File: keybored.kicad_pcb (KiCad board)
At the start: 2 copper layers, 316.7 x 133.3 mm, 202 parts, among them J1 USB_C_Receptacle_USB2.0, J2 ISP, J3 Conn_01x03, J4 Conn_01x03, K1 KEYSW, K10 KEYSW, K11 KEYSW, K12 KEYSW, K13 KEYSW, K14 KEYSW, K15 KEYSW, K16 KEYSW, K17 KEYSW, K18 KEYSW, K19 KEYSW, K2 KEYSW, K20 KEYSW, K21 KEYSW, K22 KEYSW, K23 KEYSW, K24 KEYSW, K25 KEYSW, K26 KEYSW, K27 KEYSW, K28 KEYSW, K29 KEYSW, K3 KEYSW, K30 KEYSW, K31 KEYSW, K32 KEYSW, K33 KEYSW, K34 KEYSW, K35 KEYSW, K36 KEYSW, K37 KEYSW, K38 KEYSW, K39 KEYSW, K4 KEYSW, K40 KEYSW, K41 KEYSW, K42 KEYSW, K43 KEYSW, K44 KEYSW, K45 KEYSW, K46 KEYSW, K47 KEYSW, K48 KEYSW, K49 KEYSW, K5 KEYSW, K50 KEYSW, K51 KEYSW, K52 KEYSW, K53 KEYSW, K54 KEYSW, K55 KEYSW, K56 KEYSW, K57 KEYSW, K58 KEYSW, K59 KEYSW, K6 KEYSW, K60 KEYSW, K61 KEYSW, K62 KEYSW, K63 KEYSW, K64 KEYSW, K65 KEYSW, K66 KEYSW, K7 KEYSW, K8 KEYSW, K9 KEYSW, SW1 SW_PUSH, SW2 Rot_Enc_Sw, U1 ATMEGA32U4, U2 SSD1306-Display_Graphic, Y1 Crystal

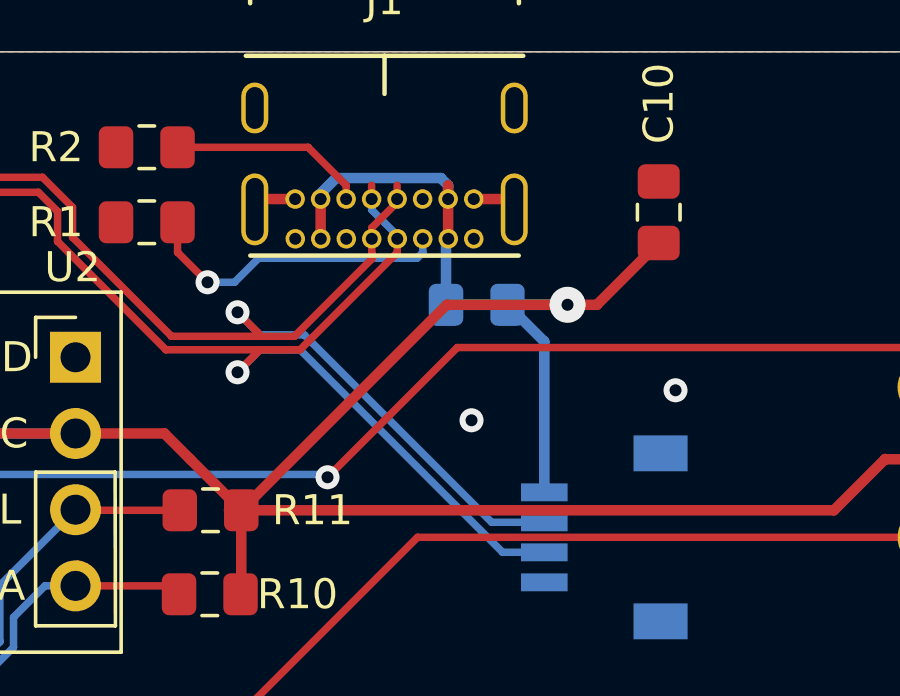
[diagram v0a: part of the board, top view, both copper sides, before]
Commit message: Updates to keyboard PCB and Plate
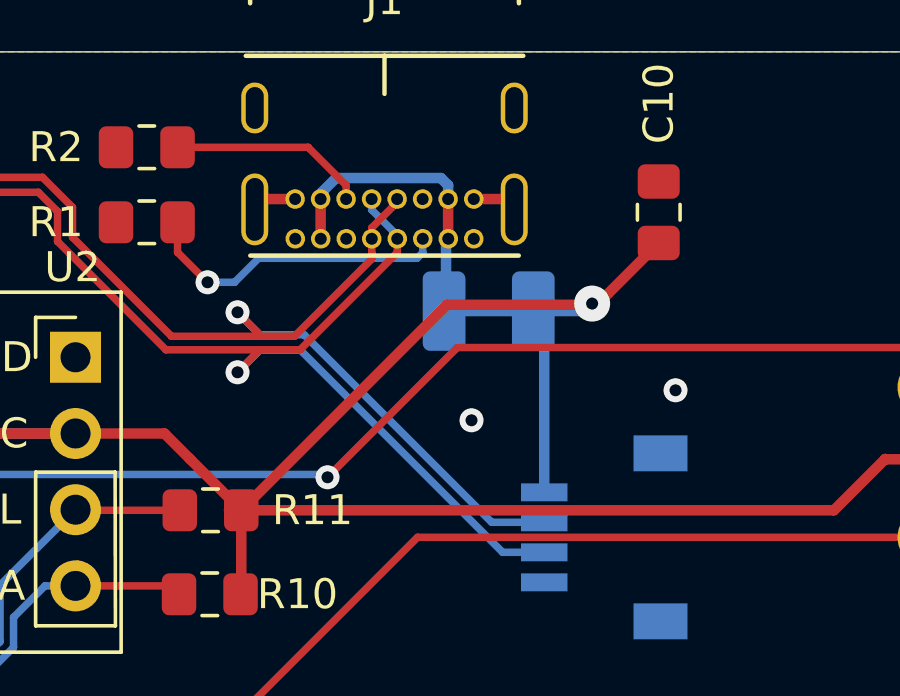
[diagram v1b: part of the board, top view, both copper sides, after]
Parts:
- removed the REF** at (340.0, 82.2)
- added REF**: Polyfuse, Fuse:Fuse_1210_3225Metric_Pad1.42x2.65mm_HandSolder, B.Cu at (340.4, 82.5)
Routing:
- net VCC: track 1050.1 -> 1048.9 mm
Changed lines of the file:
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@@
     (thickness 1.6)
     (drawings 108)
-    (tracks 2958)
+    (tracks 2956)
     (zones 0)
     (modules 202)
@@
     (mod_text_size 1 1)
     (mod_text_width 0.15)
-    (pad_size 1.15 1.4)
+    (pad_size 1.425 2.65)
     (pad_drill 0)
     (pad_to_mask_clearance 0.05)
@@
     (add_net VCC)
   )
+  (module Fuse:Fuse_1210_3225Metric_Pad1.42x2.65mm_HandSolder (layer B.Cu)
+    (at 340.3725 82.46)
+    (descr "Fuse SMD 1210 (3225 Metric), square (rectangular) end terminal, IPC_7351 nominal with elongated pad for handsoldering. (Body size source: http://www.tortai-tech.com/upload/download/2011102023233369053.pdf), generated with kicad-footprint-generator")
+    (tags "resistor handsolder")
+    (attr smd)
+    (fp_text reference REF** (at 0 2.28) (layer B.SilkS) hide
+      (effects (font (size 1 1) (thickness 0.15)) (justify mirror))
+    )
+    (fp_text value Polyfuse (at 0 -2.28) (layer B.Fab)
+      (effects (font (size 1 1) (thickness 0.15)) (justify mirror))
+    )
+    (fp_line (start 2.45 -1.58) (end -2.45 -1.58) (layer B.CrtYd) (width 0.05))
+    (fp_line (start 2.45 1.58) (end 2.45 -1.58) (layer B.CrtYd) (width 0.05))
+    (fp_line (start -2.45 1.58) (end 2.45 1.58) (layer B.CrtYd) (width 0.05))
+    (fp_line (start -2.45 -1.58) (end -2.45 1.58) (layer B.CrtYd) (width 0.05))
+    (fp_line (start -0.602064 -1.36) (end 0.602064 -1.36) (layer B.SilkS) (width 0.12))
+    (fp_line (start -0.602064 1.36) (end 0.602064 1.36) (layer B.SilkS) (width 0.12))
+    (fp_line (start 1.6 -1.25) (end -1.6 -1.25) (layer B.Fab) (width 0.1))
+    (fp_line (start 1.6 1.25) (end 1.6 -1.25) (layer B.Fab) (width 0.1))
+    (fp_line (start -1.6 1.25) (end 1.6 1.25) (layer B.Fab) (width 0.1))
+    (fp_line (start -1.6 -1.25) (end -1.6 1.25) (layer B.Fab) (width 0.1))
+    (fp_text user %R (at 0 0) (layer B.Fab)
+      (effects (font (size 0.8 0.8) (thickness 0.12)) (justify mirror))
+    )
+    (pad 2 smd roundrect (at 1.4875 0) (size 1.425 2.65) (layers B.Cu B.Paste B.Mask) (roundrect_rratio 0.175)
+      (net 77 VCC))
+    (pad 1 smd roundrect (at -1.4875 0) (size 1.425 2.65) (layers B.Cu B.Paste B.Mask) (roundrect_rratio 0.175439)
+      (net 77 VCC))
+    (model ${KISYS3DMOD}/Fuse.3dshapes/Fuse_1210_3225Metric.wrl
+      (at (xyz 0 0 0))
+      (scale (xyz 1 1 1))
+      (rotate (xyz 0 0 0))
+    )
+  )
   (module keybored:floppy_disks_2 (layer B.Cu)
     (at 255 83.75 180)
@@
       (net 79 USB_D+))
   )
-  (module Fuse:Fuse_0805_2012Metric_Pad1.15x1.40mm_HandSolder locked (layer B.Cu)
-    (at 339.975 82.25)
-    (descr "Fuse SMD 0805 (2012 Metric), square (rectangular) end terminal, IPC_7351 nominal with elongated pad for handsoldering. (Body size source: https://docs.google.com/spreadsheets/d/1BsfQQcO9C6DZCsRaXUlFlo91Tg2WpOkGARC1WS5S8t0/edit?usp=sharing), generated with kicad-footprint-generator")
-    (tags "resistor handsolder")
-    (attr smd)
-    (fp_text reference REF** (at 4 0) (layer B.SilkS) hide
-      (effects (font (size 1 1) (thickness 0.15)) (justify mirror))
-    )
-    (fp_text value Fuse_0805 (at 0 -1.5) (layer B.Fab) hide
-      (effects (font (size 1 1) (thickness 0.15)) (justify mirror))
-    )
-    (fp_line (start -1 -0.6) (end -1 0.6) (layer B.Fab) (width 0.1))
-    (fp_line (start -1 0.6) (end 1 0.6) (layer B.Fab) (width 0.1))
-    (fp_line (start 1 0.6) (end 1 -0.6) (layer B.Fab) (width 0.1))
-    (fp_line (start 1 -0.6) (end -1 -0.6) (layer B.Fab) (width 0.1))
-    (fp_line (start -0.261252 0.71) (end 0.261252 0.71) (layer B.SilkS) (width 0.12))
-    (fp_line (start -0.261252 -0.71) (end 0.261252 -0.71) (layer B.SilkS) (width 0.12))
-    (fp_line (start -1.85 -0.95) (end -1.85 0.95) (layer B.CrtYd) (width 0.05))
-    (fp_line (start -1.85 0.95) (end 1.85 0.95) (layer B.CrtYd) (width 0.05))
-    (fp_line (start 1.85 0.95) (end 1.85 -0.95) (layer B.CrtYd) (width 0.05))
-    (fp_line (start 1.85 -0.95) (end -1.85 -0.95) (layer B.CrtYd) (width 0.05))
-    (fp_text user %R (at 0 0) (layer B.Fab)
-      (effects (font (size 0.5 0.5) (thickness 0.08)) (justify mirror))
-    )
-    (pad 2 smd roundrect (at 1.025 0) (size 1.15 1.4) (layers B.Cu B.Paste B.Mask) (roundrect_rratio 0.217)
-      (net 77 VCC))
-    (pad 1 smd roundrect (at -1.025 0) (size 1.15 1.4) (layers B.Cu B.Paste B.Mask) (roundrect_rratio 0.217)
-      (net 77 VCC))
-    (model ${KISYS3DMOD}/Fuse.3dshapes/Fuse_0805_2012Metric.wrl
-      (at (xyz 0 0 0))
-      (scale (xyz 1 1 1))
-      (rotate (xyz 0 0 0))
-    )
-  )
   (module keybored:sadge_decal (layer B.Cu)
     (at 160.5 193.5 180)
@@
   (gr_circle (center 216.69375 214.3125) (end 219.075 214.3125) (layer Dwgs.User) (width 0.15))
   (gr_circle (center 100.0125 214.3125) (end 102.39375 214.3125) (layer Dwgs.User) (width 0.15))
-  (gr_text GND (at 316.3 99.2 90) (layer B.SilkS)
+  (gr_text GND (at 311 99.2 90) (layer B.SilkS)
     (effects (font (size 1 1) (thickness 0.15)) (justify mirror))
   )
@@
     (effects (font (size 1 1) (thickness 0.15)) (justify mirror))
   )
-  (gr_text +5V (at 311.3 99.1 90) (layer B.SilkS)
+  (gr_text +5V (at 316.2 99.1 90) (layer B.SilkS)
     (effects (font (size 1 1) (thickness 0.15)) (justify mirror))
   )
@@
   (segment (start 106.75 104.05) (end 111.46999 108.76999) (width 0.25) (layer B.Cu) (net 76))
   (segment (start 106.75 99.29) (end 106.75 104.05) (width 0.25) (layer B.Cu) (net 76))
-  (via (at 343 82.25) (size 1.2) (drill 0.4) (layers F.Cu B.Cu) (net 77))
+  (via (at 343.82 82.21) (size 1.2) (drill 0.4) (layers F.Cu B.Cu) (net 77))
   (segment (start 282.99325 88.032233) (end 283.477359 87.548124) (width 0.25) (layer F.Cu) (net 77))
   (segment (start 269.922641 92.051876) (end 270.40675 91.567767) (width 0.25) (layer F.Cu) (net 77))
@@
   (segment (start 334.77 78.725) (end 334.77 80.045) (width 0.35) (layer F.Cu) (net 77))
   (segment (start 346.04 79.81826) (end 346.04 80.19) (width 0.35) (layer F.Cu) (net 77))
-  (segment (start 339.02 78.725) (end 339.02 78.265381) (width 0.35) (layer F.Cu) (net 77))
   (segment (start 293.234999 78.424999) (end 291.92 77.11) (width 0.35) (layer B.Cu) (net 77))
   (segment (start 293.234999 81.384999) (end 293.234999 78.424999) (width 0.35) (layer B.Cu) (net 77))
@@
   (segment (start 338.95 80.125) (end 339.025 80.05) (width 0.35) (layer B.Cu) (net 77))
   (segment (start 338.95 82.25) (end 338.997002 82.25) (width 0.35) (layer B.Cu) (net 77))
-  (segment (start 338.95 82.25) (end 341 82.25) (width 0.35) (layer B.Cu) (net 77))
-  (segment (start 342.225 83.475) (end 341 82.25) (width 0.35) (layer B.Cu) (net 77))
   (segment (start 342.225 88.5) (end 342.225 83.475) (width 0.35) (layer B.Cu) (net 77))
   (segment (start 338.95 82.25) (end 338.95 80.125) (width 0.35) (layer B.Cu) (net 77))
-  (segment (start 343 82.25) (end 341 82.25) (width 0.35) (layer B.Cu) (net 77))
-  (segment (start 338.975 82.25) (end 332.125 89.1) (width 0.35) (layer F.Cu) (net 77))
-  (segment (start 343 82.25) (end 338.975 82.25) (width 0.35) (layer F.Cu) (net 77))
-  (segment (start 343.98 82.25) (end 346.04 80.19) (width 0.35) (layer F.Cu) (net 77))
-  (segment (start 343 82.25) (end 343.98 82.25) (width 0.35) (layer F.Cu) (net 77))
+  (segment (start 338.885 82.46) (end 341.86 82.46) (width 0.35) (layer B.Cu) (net 77))
+  (segment (start 343.57 82.46) (end 343.82 82.21) (width 0.35) (layer B.Cu) (net 77))
+  (segment (start 341.86 82.46) (end 343.57 82.46) (width 0.35) (layer B.Cu) (net 77))
+  (segment (start 343.78 82.25) (end 343.82 82.21) (width 0.35) (layer F.Cu) (net 77))
+  (segment (start 332.125 89.1) (end 338.975 82.25) (width 0.35) (layer F.Cu) (net 77))
+  (segment (start 338.975 82.25) (end 343.78 82.25) (width 0.35) (layer F.Cu) (net 77))
+  (segment (start 344.02 82.21) (end 346.04 80.19) (width 0.35) (layer F.Cu) (net 77))
+  (segment (start 343.82 82.21) (end 344.02 82.21) (width 0.35) (layer F.Cu) (net 77))
   (segment (start 335.475 78.725) (end 335.420001 78.670001) (width 0.25) (layer B.Cu) (net 78))
   (segment (start 335.62 78.725) (end 335.475 78.725) (width 0.25) (layer B.Cu) (net 78))
@@
   (segment (start 337.325 80.05) (end 337.325 79.937998) (width 0.25) (layer B.Cu) (net 79))
   (segment (start 336.47 78.725) (end 336.47 78.612998) (width 0.25) (layer F.Cu) (net 79))
-  (segment (start 336.47 78.725) (end 336.47 78.265381) (width 0.25) (layer F.Cu) (net 79))
   (segment (start 337.325 80.05) (end 337.325 80.296029) (width 0.25) (layer F.Cu) (net 79))
   (via (at 332 84.5) (size 0.8) (drill 0.4) (layers F.Cu B.Cu) (net 79))
@@
   (segment (start 337.32 78.725) (end 337.32 78.612998) (width 0.25) (layer F.Cu) (net 80))
   (segment (start 322.094981 77.094981) (end 322 77) (width 0.25) (layer F.Cu) (net 80))
-  (segment (start 337.32 78.725) (end 337.32 78.265381) (width 0.25) (layer F.Cu) (net 80))
   (via (at 332 82.5) (size 0.8) (drill 0.4) (layers F.Cu B.Cu) (net 80))
   (segment (start 336.475 80.723209) (end 336.475 80.509619) (width 0.25) (layer F.Cu) (net 80))
